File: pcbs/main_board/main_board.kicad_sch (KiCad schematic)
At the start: 9 parts, among them J3 LED strip, J4 Motor, U1 mini_esp32, U6 TPS22917LDBV

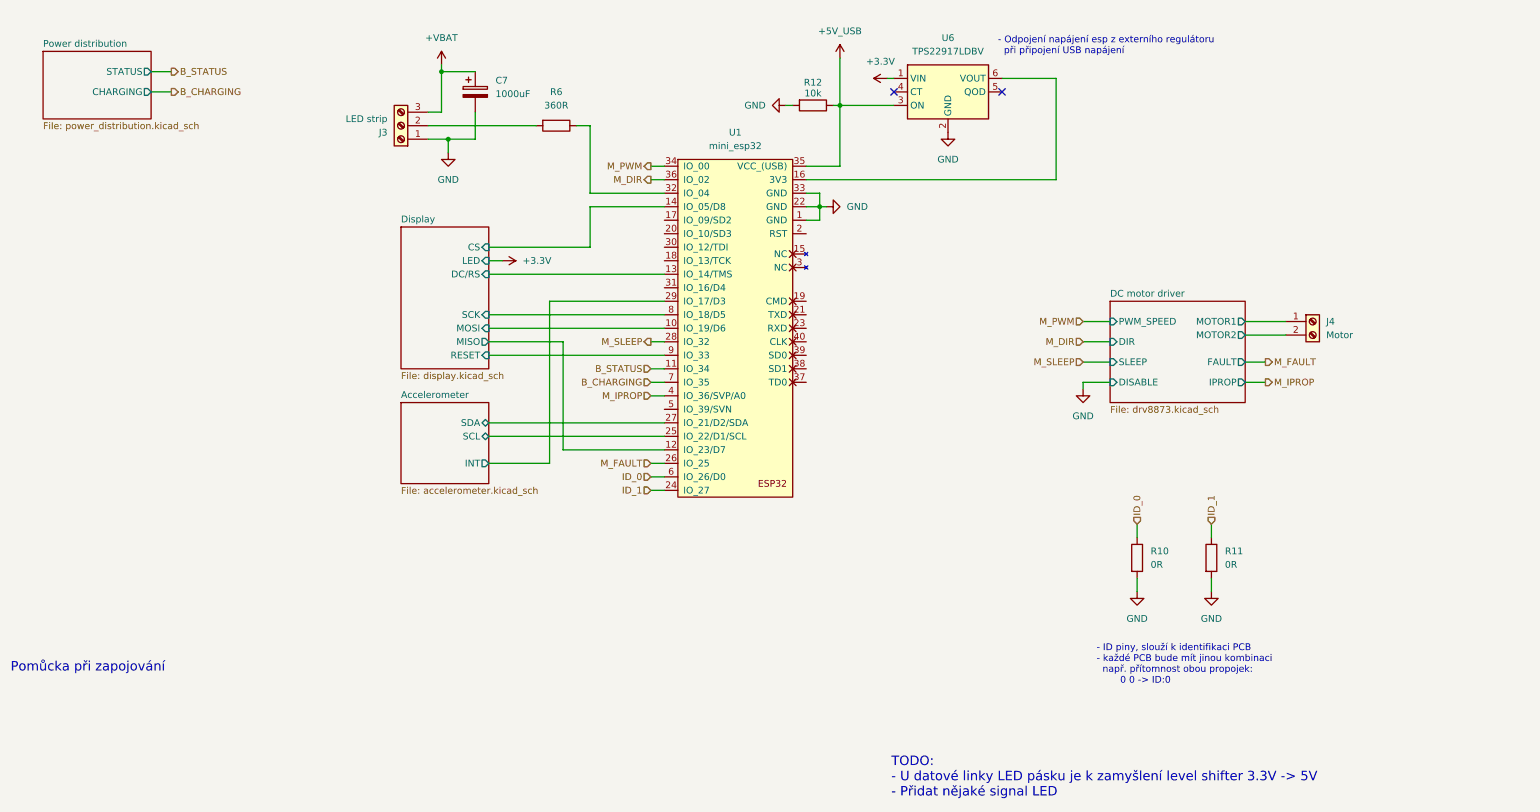
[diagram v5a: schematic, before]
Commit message: Add edge cuts and notes to pcb
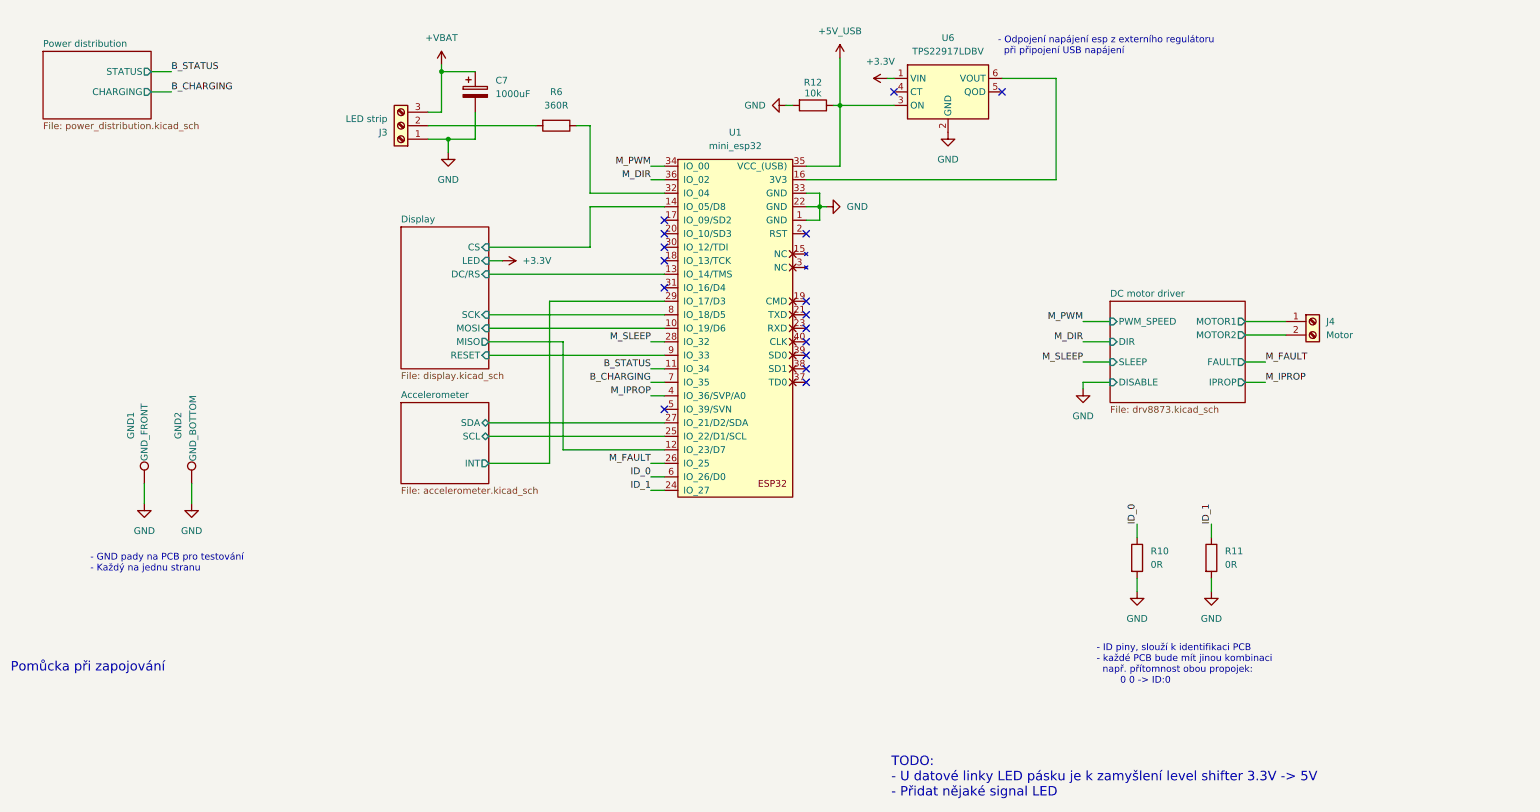
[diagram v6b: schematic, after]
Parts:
- added GND1: GND_FRONT, TestPoint:TestPoint_Pad_1.5x1.5mm, symbol Connector:TestPoint
- added GND2: GND_BOTTOM, TestPoint:TestPoint_Pad_1.5x1.5mm, symbol Connector:TestPoint
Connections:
- net GND: now also GND1.1, GND2.1
- no-connect marks 2 -> 16
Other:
- note added: "- GND pady na PCB pro testování - Každý na jednu stranu"

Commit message: Change 3V3 regulator, add level shifter for led strip
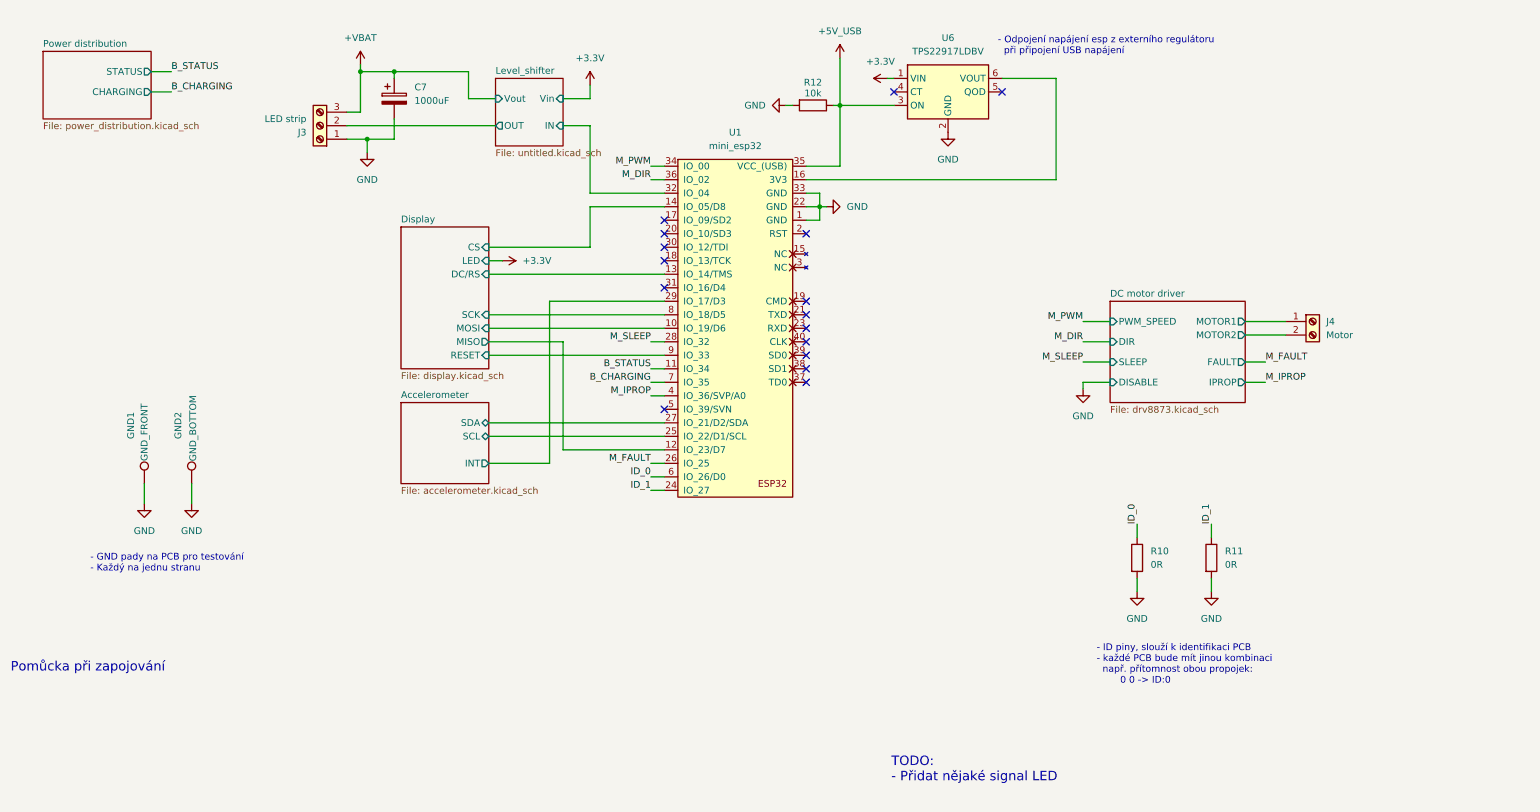
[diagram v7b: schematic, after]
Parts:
- removed R6: 360R, Resistor_SMD:R_0603_1608Metric_Pad0.98x0.95mm_HandSolder, symbol Device:R
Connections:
- net Level_shifter/IN: now reaches U1.32 (IO_04)
- net Level_shifter/OUT: now reaches J3.2 (Pin_2)
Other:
- added sheet Level_shifter (untitled.kicad_sch)
- note added: "TODO: - Přidat nějaké signal LED"
- note removed: "TODO: - U datové linky LED pásku je k zamyšlení level shifter 3.3V -> 5V - Přidat nějaké signal LED"
- moved on the sheet: C7, J3

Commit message: Add LED indicators
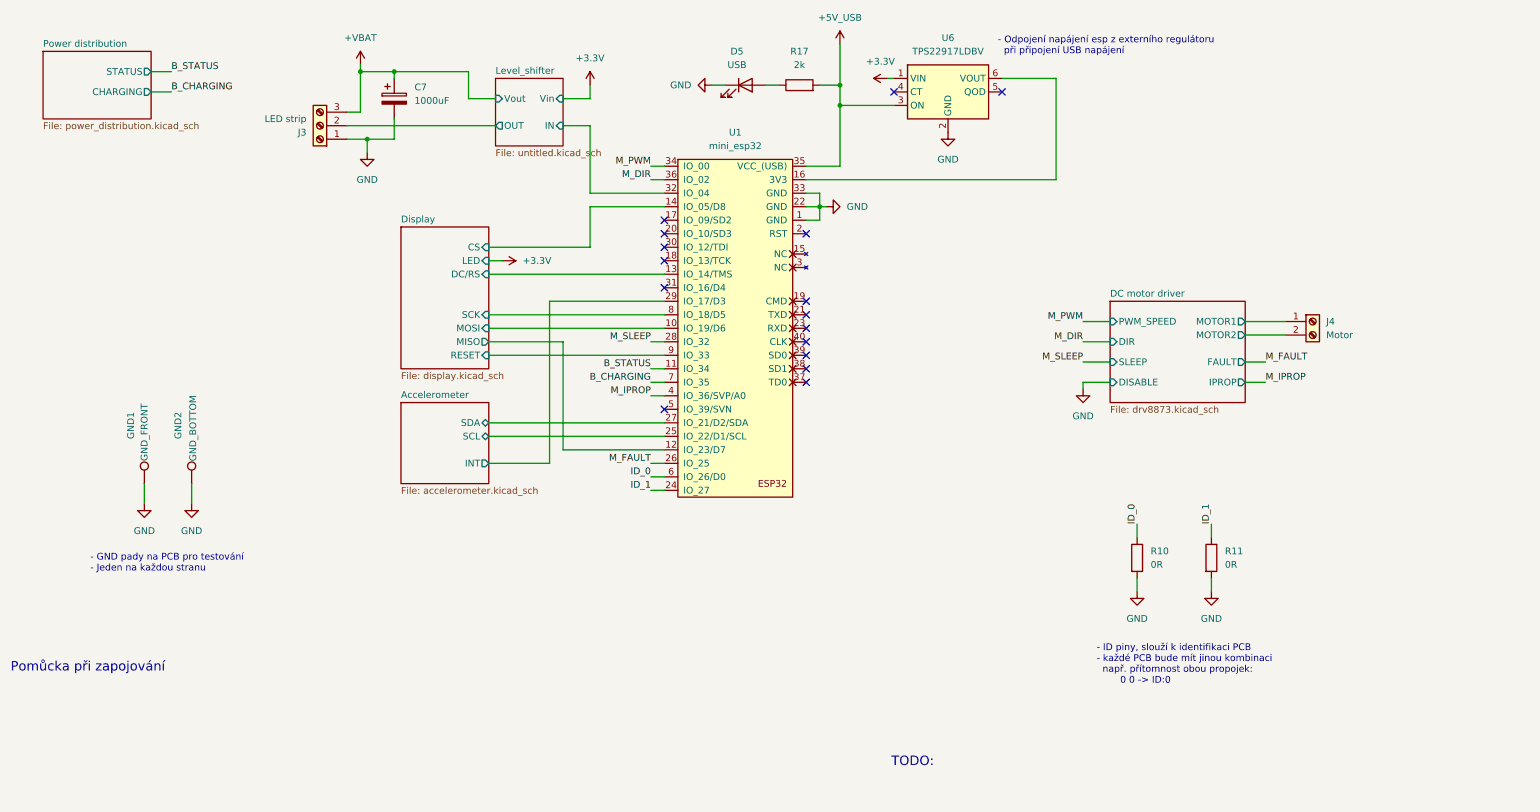
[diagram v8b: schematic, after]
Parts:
- removed R12: 10k, Resistor_SMD:R_0603_1608Metric_Pad0.98x0.95mm_HandSolder, symbol Device:R
- added D5: USB, LED_SMD:LED_0805_2012Metric_Pad1.15x1.40mm_HandSolder, symbol Device:LED
- added R17: 2k, Resistor_SMD:R_0603_1608Metric_Pad0.98x0.95mm_HandSolder, symbol Device:R
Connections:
- net +5V_USB: now also R17.2
- net GND: now also D5.1 (K)
- new net: D5.2 (A), R17.1
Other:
- note added: "- GND pady na PCB pro testování - Jeden na každou stranu"
- note added: "TODO:"
- note removed: "- GND pady na PCB pro testování - Každý na jednu stranu"
- note removed: "TODO: - Přidat nějaké signal LED"
